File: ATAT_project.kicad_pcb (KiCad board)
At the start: 2 copper layers, 26 parts, among them SW1 SW_Push, SW2 SW_Push, U1 STM32F446RETx, U2 SPBTLE-RF

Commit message: scuffed but done
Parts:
- removed TP2: Test_VDDA, TestPoint:TestPoint_Keystone_5010-5014_Multipurpose
- added C12: 100p, Capacitor_SMD:C_0805_2012Metric_Pad1.18x1.45mm_HandSolder, F.Cu at (135.3, 50.7)
- added C13: 1u, Capacitor_SMD:C_0805_2012Metric_Pad1.18x1.45mm_HandSolder, F.Cu at (140.6, 50.7)
- added G***: LOGO, test:test5, F.Cu at (98.0, 57.7)
- C8: moved to F.Cu
- moved UART1 52.9 mm to (99.0, 83.4), turned to 90 degrees
- moved PWM_Channels1 50.4 mm to (89.9, 76.4), turned to 180 degrees
- moved U2 46.8 mm to (135.4, 56.0), turned to 180 degrees
- moved TP1 37.2 mm to (125.5, 70.0)
- moved TP5 30.9 mm to (114.3, 75.2)
- moved TP7 26.4 mm to (121.4, 74.3)
- moved TP3 26.1 mm to (95.0, 83.4)
- moved SW2 25.1 mm to (131.9, 83.7)
- moved TP6 23.8 mm to (107.1, 75.4)
- moved TP4 21.7 mm to (90.5, 83.4)
- moved SW1 16.9 mm to (142.3, 83.6)
- moved 2x5_stlinkv2 15.0 mm to (110.3, 83.3)
- moved C3 5.79 mm to (112.0, 59.5)
- moved C11 3.41 mm to (107.6, 56.1)
- moved C9 2.91 mm to (121.9, 60.9), turned to -90 degrees
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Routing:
- net +3V3: track 0.00 -> 142.0 mm, vias 0 -> 11
- net Net-(PWM_Channels1-Pin_10): track 0.00 -> 58.6 mm, vias 0 -> 3
- net Net-(PWM_Channels1-Pin_1): track 0.00 -> 43.3 mm, vias 0 -> 1
- net Net-(U1-PC2): track 0.00 -> 36.9 mm, vias 0 -> 1
- net Net-(PWM_Channels1-Pin_4): track 0.00 -> 36.8 mm, vias 0 -> 1
- net Net-(U1-PB10): track 0.00 -> 36.6 mm, vias 0 -> 2
- net Net-(PWM_Channels1-Pin_9): track 0.00 -> 36.3 mm, vias 0 -> 3
- net Net-(PWM_Channels1-Pin_2): track 0.00 -> 35.3 mm
- net Net-(PWM_Channels1-Pin_3): track 0.00 -> 34.4 mm, vias 0 -> 1
- net Net-(PWM_Channels1-Pin_5): track 0.00 -> 31.6 mm, vias 0 -> 1
- net Net-(U1-NRST): track 0.00 -> 31.4 mm
- net Net-(PWM_Channels1-Pin_6): track 0.00 -> 27.5 mm, vias 0 -> 1
- net Net-(U1-PA7): track 0.00 -> 24.6 mm, vias 0 -> 2
- net /swdio: track 0.00 -> 23.8 mm, vias 0 -> 2
- net Net-(U1-PB12): track 0.00 -> 23.6 mm, vias 0 -> 2
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- added copper zone on B.Cu, net GND
- added copper zone on F.Cu, net GND
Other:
- board outline added: 56.2 x 37.9 mm

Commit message: Fixed all DRC, started Casey's feedback
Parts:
- removed TP5: Test_swdio, TestPoint:TestPoint_Keystone_5010-5014_Multipurpose
- removed TP6: Test_swclk, TestPoint:TestPoint_Keystone_5010-5014_Multipurpose
- added GND1: Test_GND, TestPoint:TestPoint_Keystone_5010-5014_Multipurpose, F.Cu at (112.8, 74.6)
- added R1: 10k, Resistor_SMD:R_0805_2012Metric_Pad1.20x1.40mm_HandSolder, F.Cu at (138.0, 86.0)
- added R2: 10k, Resistor_SMD:R_0805_2012Metric_Pad1.20x1.40mm_HandSolder, F.Cu at (133.5, 86.0)
- PWM_Channels1: footprint Connector_PinHeader_2.54mm:PinHeader_1x11_P2.54mm_Vertical -> Connector_PinSocket_2.54mm:PinSocket_1x11_P2.54mm_Vertical
- UART1: value Conn_01x03_Female -> Conn_01x06_Socket; footprint Connector_PinHeader_2.54mm:PinHeader_1x03_P2.54mm_Vertical -> Connector_PinSocket_2.54mm:PinSocket_1x06_P2.54mm_Vertical
- moved RX1 16.3 mm to (105.3, 76.6)
- moved TX1 7.82 mm to (101.8, 79.6)
- moved UART1 2.91 mm to (101.8, 84.1), turned to -90 degrees
- moved C8 2.31 mm to (119.3, 57.6)
- moved FB1 2.06 mm to (122.8, 58.6)
- moved C6 2.05 mm to (116.8, 69.8)
- moved U2 2.05 mm to (133.6, 57.1)
- moved C12 2.05 mm to (133.6, 51.8)
- moved C13 2.05 mm to (138.9, 51.8)
- moved C4 2.05 mm to (115.1, 57.7)
- moved VDD1 2.05 mm to (123.7, 71.1)
- moved Button1 2.05 mm to (119.7, 75.4)
- moved C1 2.05 mm to (119.9, 66.1)
- moved C2 2.05 mm to (116.3, 54.2)
- moved C3 2.05 mm to (110.3, 60.6)
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- renumbered TP7 to Button1, SW1 to RESET1, TP4 to RX1, SW2 to Start/Stop1, TP3 to TX1, TP1 to VDD1, 2x5_stlinkv2 to stlinkv2
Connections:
- C7 pad 1: +3V3 -> Net-(C7-Pad1)
- C8 pad 1: +3V3 -> Net-(C7-Pad1)
- C9 pad 1: Net-(C9-Pad1) -> Net-(C7-Pad1)
- FB1 pad 2: Net-(C9-Pad1) -> Net-(C7-Pad1)
- UART1 pad 1: /TX -> unconnected-(UART1-Pin_1-Pad1)
- UART1 pad 3: GND -> /TX
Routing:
- net GND: track 22.0 -> 127.0 mm, vias 7 -> 13
- net /RX: track 0.00 -> 38.2 mm, vias 0 -> 2
- net /TX: track 0.00 -> 34.0 mm, vias 0 -> 2
- net Net-(C7-Pad1): track 0.00 -> 16.2 mm, vias 0 -> 3
- net Net-(PWM_Channels1-Pin_9): track 36.3 -> 46.2 mm
- net Net-(PWM_Channels1-Pin_10): track 58.6 -> 49.3 mm, vias 3 -> 1
- net Net-(U1-NRST): track 31.4 -> 39.3 mm
- net Net-(C9-Pad1): track 3.60 -> 0.00 mm
- net Net-(U1-PB12): track 23.6 -> 26.5 mm
- net +3V3: track 142.0 -> 139.4 mm, vias 11 -> 9
- net +3.3V: track 0.00 -> 2.50 mm
- net Net-(U1-PA5): track 23.6 -> 22.0 mm
- net /swclk: track 14.7 -> 16.0 mm
- net Net-(PWM_Channels1-Pin_1): track 43.3 -> 42.0 mm
- net Net-(U1-PC2): track 36.9 -> 37.9 mm
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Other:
- board text added: "ATAT Walker PCB ECE395 Fall 2024 Joseph C, Eddie D, Frank F"

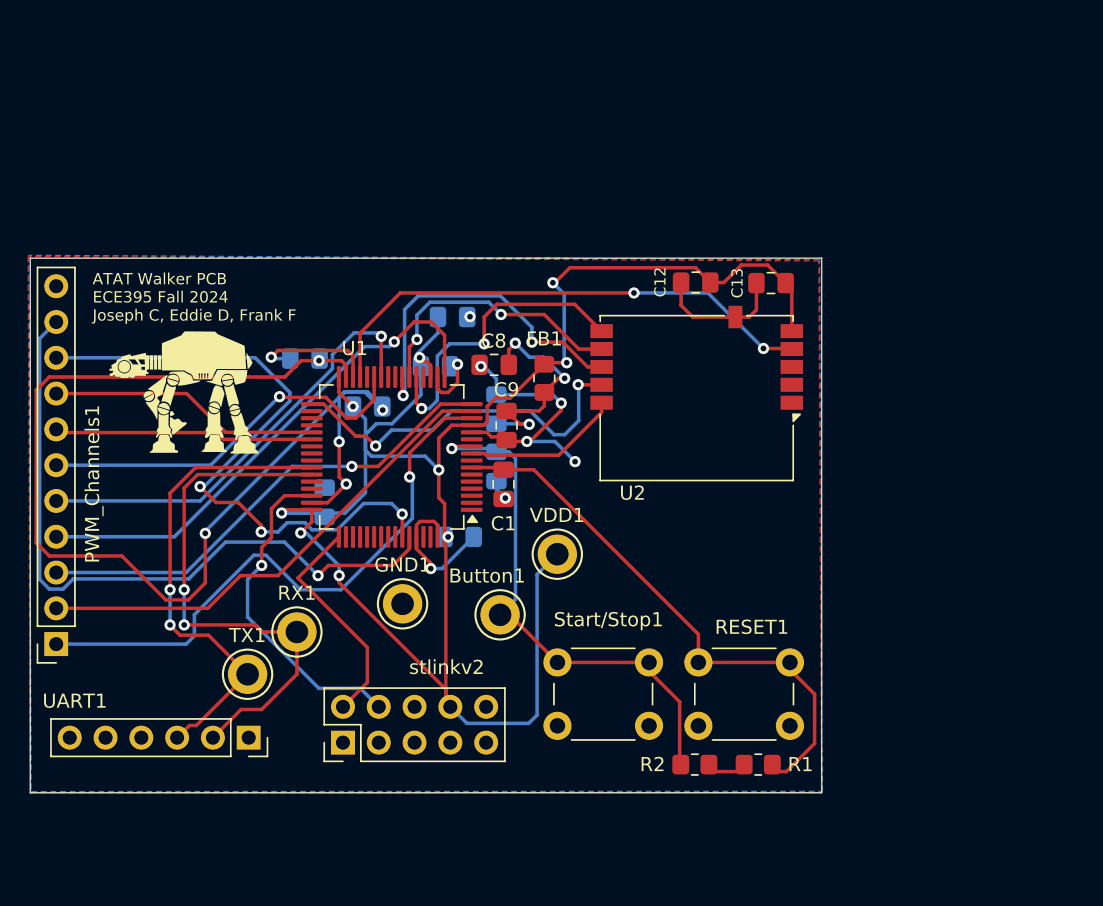
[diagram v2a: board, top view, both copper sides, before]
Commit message: NEW SCHEMATIC! (Needs PCB Design)
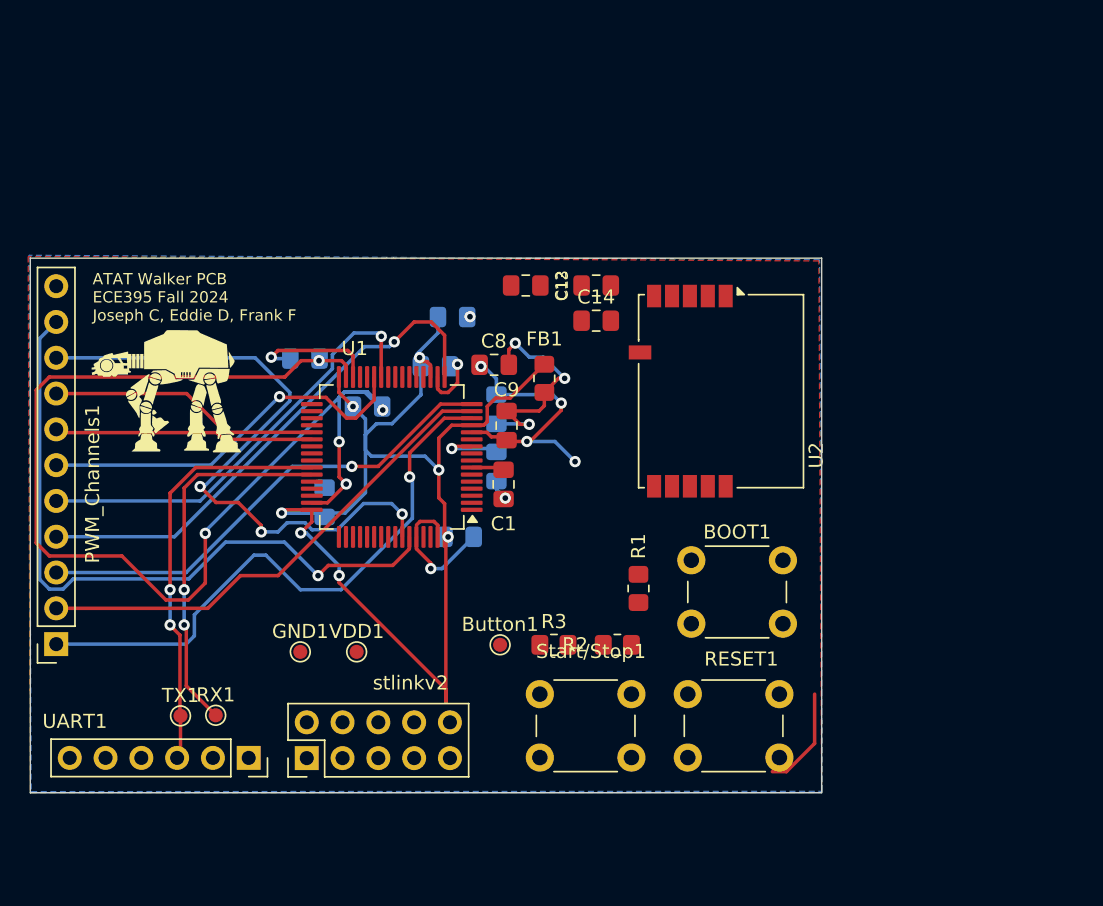
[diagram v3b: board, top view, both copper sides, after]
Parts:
- added BOOT1: SW_Push, Button_Switch_THT:SW_PUSH_6mm_H4.3mm, F.Cu at (133.2, 71.5)
- added C14: 0.1u, Capacitor_SMD:C_0805_2012Metric_Pad1.18x1.45mm_HandSolder, F.Cu at (126.5, 54.5)
- added R3: 10k, Resistor_SMD:R_0805_2012Metric_Pad1.20x1.40mm_HandSolder, F.Cu at (123.5, 77.5)
- Button1, GND1, RX1, TX1, VDD1: footprint TestPoint:TestPoint_Keystone_5010-5014_Multipurpose -> TestPoint:TestPoint_Pad_D1.0mm
- moved VDD1 15.8 mm to (109.5, 78.0)
- moved R1 15.1 mm to (129.5, 73.5), turned to 90 degrees
- moved C13 12.4 mm to (126.5, 52.0)
- moved C12 12.1 mm to (121.5, 52.0), turned to 180 degrees
- moved R2 10.1 mm to (128.0, 77.5)
- moved RX1 8.25 mm to (99.5, 82.5)
- moved GND1 8.02 mm to (105.5, 78.0)
- moved TX1 5.60 mm to (97.0, 82.5)
- moved stlinkv2 2.80 mm to (106.0, 85.5)
- moved U2 2.63 mm to (132.5, 59.5), turned to -90 degrees
- moved Start/Stop1 2.57 mm to (129.0, 85.5)
- moved RESET1 2.37 mm to (139.5, 85.5)
- moved Button1 2.13 mm to (119.7, 77.5)
- moved UART1 1.44 mm to (101.8, 85.5)
- moved G*** 1.26 mm to (96.0, 59.5)
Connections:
- C7 pad 1: Net-(C7-Pad1) -> +3V3
- C8 pad 1: Net-(C7-Pad1) -> +3V3
- C9 pad 1: Net-(C7-Pad1) -> +3V3
- FB1 pad 2: Net-(C7-Pad1) -> +3V3
- U1 pad 1: unconnected-(U1-VBAT-Pad1) -> +3V3
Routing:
- net Net-(U1-NRST): track 39.3 -> 2.32 mm
- net Net-(U1-PB10): track 36.6 -> 0.00 mm, vias 2 -> 0
- net Net-(U1-PC2): track 37.9 -> 4.75 mm
- net +3V3: track 139.4 -> 106.3 mm, vias 9 -> 10
- net Net-(U1-PB12): track 26.5 -> 0.00 mm, vias 2 -> 0
- net Net-(U1-PA7): track 24.6 -> 0.00 mm, vias 2 -> 0
- net /swdio: track 23.6 -> 0.00 mm, vias 1 -> 0
- net Net-(U1-PA5): track 22.0 -> 0.00 mm, vias 2 -> 0
- net Net-(U1-PA6): track 19.5 -> 0.00 mm, vias 2 -> 0
- net Net-(C7-Pad1): track 16.2 -> 0.00 mm, vias 3 -> 0
- net /swclk: track 16.0 -> 0.00 mm
- net /RX: track 38.2 -> 26.2 mm
- net Net-(U1-PC1): track 11.2 -> 0.00 mm
- net /TX: track 34.0 -> 29.9 mm
- net +3.3V: track 2.50 -> 0.00 mm
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
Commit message: NEW PCB!!!
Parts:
- removed PWM_Channels1: Conn_01x11_Female, Connector_PinSocket_2.54mm:PinSocket_1x11_P2.54mm_Vertical
- added 5V1: Test_5V, TestPoint:TestPoint_Pad_D1.0mm, F.Cu at (151.5, 54.5)
- added C15: 100n, Capacitor_SMD:C_0805_2012Metric_Pad1.18x1.45mm_HandSolder, F.Cu at (109.0, 65.5)
- added J1: Conn_01x03_Socket, Connector_PinSocket_2.54mm:PinSocket_1x03_P2.54mm_Vertical, F.Cu at (155.5, 49.0)
- added PWM1: Conn_01x03_Pin, Connector_PinHeader_2.54mm:PinHeader_1x03_P2.54mm_Vertical, F.Cu at (142.0, 54.0)
- added PWM10: Conn_01x03_Pin, Connector_PinHeader_2.54mm:PinHeader_1x03_P2.54mm_Vertical, F.Cu at (100.2, 54.0)
- added PWM2: Conn_01x03_Pin, Connector_PinHeader_2.54mm:PinHeader_1x03_P2.54mm_Vertical, F.Cu at (137.3, 54.0)
- added PWM3: Conn_01x03_Pin, Connector_PinHeader_2.54mm:PinHeader_1x03_P2.54mm_Vertical, F.Cu at (132.7, 54.0)
- added PWM4: Conn_01x03_Pin, Connector_PinHeader_2.54mm:PinHeader_1x03_P2.54mm_Vertical, F.Cu at (128.1, 54.0)
- added PWM5: Conn_01x03_Pin, Connector_PinHeader_2.54mm:PinHeader_1x03_P2.54mm_Vertical, F.Cu at (123.4, 54.0)
- added PWM6: Conn_01x03_Pin, Connector_PinHeader_2.54mm:PinHeader_1x03_P2.54mm_Vertical, F.Cu at (118.8, 54.0)
- added PWM7: Conn_01x03_Pin, Connector_PinHeader_2.54mm:PinHeader_1x03_P2.54mm_Vertical, F.Cu at (114.1, 54.0)
- added PWM8: Conn_01x03_Pin, Connector_PinHeader_2.54mm:PinHeader_1x03_P2.54mm_Vertical, F.Cu at (109.5, 54.0)
- added PWM9: Conn_01x03_Pin, Connector_PinHeader_2.54mm:PinHeader_1x03_P2.54mm_Vertical, F.Cu at (104.8, 54.0)
- added TP1: Test_PWM, TestPoint:TestPoint_Pad_D1.0mm, F.Cu at (142.2, 58.5)
- added TP10: Test_PWM, TestPoint:TestPoint_Pad_D1.0mm, F.Cu at (100.2, 58.5)
- added TP2: Test_PWM, TestPoint:TestPoint_Pad_D1.0mm, F.Cu at (137.7, 58.5)
- added TP3: Test_PWM, TestPoint:TestPoint_Pad_D1.0mm, F.Cu at (133.2, 58.5)
- added TP4: Test_PWM, TestPoint:TestPoint_Pad_D1.0mm, F.Cu at (128.7, 58.5)
- added TP5: Test_PWM, TestPoint:TestPoint_Pad_D1.0mm, F.Cu at (123.7, 58.5)
- added TP6: Test_PWM, TestPoint:TestPoint_Pad_D1.0mm, F.Cu at (119.2, 58.5)
- added TP7: Test_PWM, TestPoint:TestPoint_Pad_D1.0mm, F.Cu at (114.7, 58.5)
- added TP8: Test_PWM, TestPoint:TestPoint_Pad_D1.0mm, F.Cu at (110.2, 58.5)
- added TP9: Test_PWM, TestPoint:TestPoint_Pad_D1.0mm, F.Cu at (105.2, 58.5)
- C10, C11, C2, C3, C4, C5, C6, C7: moved to F.Cu
- moved GND1 53.1 mm to (151.5, 51.5), turned to 180 degrees
- moved VDD1 51.3 mm to (151.5, 48.5), turned to 180 degrees
- moved stlinkv2 48.6 mm to (154.5, 87.5), turned to -90 degrees
- moved G*** 45.4 mm to (139.0, 74.0)
- moved C14 25.5 mm to (112.0, 75.5), turned to 90 degrees
- moved C12 24.8 mm to (143.5, 63.5), turned to -90 degrees
- moved C11 23.6 mm to (116.0, 78.5)
- moved C13 20.8 mm to (145.5, 60.5)
- moved Button1 20.0 mm to (103.0, 88.5), turned to 90 degrees
- moved UART1 19.7 mm to (100.0, 65.9), turned to 0 degrees
- moved U2 19.3 mm to (148.8, 69.8)
- moved C8 19.2 mm to (136.0, 67.0), turned to -90 degrees
- moved R2 18.8 mm to (110.0, 83.0), turned to 0 degrees
- moved Start/Stop1 17.1 mm to (112.8, 90.8)
- moved RESET1 15.2 mm to (125.2, 90.8)
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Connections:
- net Net-(U1-PA5) renamed SPI_CLK
- net Net-(U1-PA6) renamed SPI_MISO
- net Net-(U1-PA7) renamed SPI_MOSI
- net Net-(U1-PB10) renamed SPI_IRQ
- net Net-(U1-PB12) renamed SPI_CS
- net Net-(U1-PC1) renamed BT_RESET
- C12 pad 2: +3V3 -> +3.3V
- C13 pad 2: +3V3 -> +3.3V
- C2 pad 1: +3V3 -> +3.3V
- C3 pad 1: +3V3 -> +3.3V
- C4 pad 1: +3V3 -> +3.3V
- C5 pad 1: +3V3 -> +3.3V
- C6 pad 1: +3V3 -> +3.3V
- C7 pad 1: +3V3 -> +3.3V
- C8 pad 1: +3V3 -> +3.3V
- C9 pad 1: +3V3 -> +3.3V
- FB1 pad 1: +3V3 -> +3.3V
- FB1 pad 2: +3V3 -> +3.3V
- RX1 pad 1: /RX -> /MCU_RX
- TX1 pad 1: /TX -> /MCU_TX
- U1 pad 1: +3V3 -> +3.3V
- U1 pad 13: +3V3 -> +3.3V
- U1 pad 14: Net-(PWM_Channels1-Pin_1) -> PWM1
- U1 pad 15: Net-(PWM_Channels1-Pin_2) -> PWM2
- U1 pad 16: Net-(PWM_Channels1-Pin_3) -> PWM3
- U1 pad 17: Net-(PWM_Channels1-Pin_4) -> PWM4
- U1 pad 19: +3V3 -> +3.3V
- U1 pad 26: Net-(PWM_Channels1-Pin_5) -> PWM5
- U1 pad 27: Net-(PWM_Channels1-Pin_6) -> PWM6
- U1 pad 32: +3V3 -> +3.3V
- U1 pad 37: Net-(PWM_Channels1-Pin_8) -> PWM8
- U1 pad 38: Net-(PWM_Channels1-Pin_7) -> PWM7
- U1 pad 42: /TX -> /MCU_TX
- U1 pad 43: /RX -> /MCU_RX
- U1 pad 48: +3V3 -> +3.3V
- U1 pad 58: Net-(PWM_Channels1-Pin_9) -> PWM9
- U1 pad 59: Net-(PWM_Channels1-Pin_10) -> PWM10
- U1 pad 64: +3V3 -> +3.3V
- U2 pad 5: +3V3 -> +3.3V
- UART1 pad 1: unconnected-(UART1-Pin_1-Pad1) -> GND
- UART1 pad 2: /RX -> unconnected-(UART1-Pin_2-Pad2)
- UART1 pad 3: /TX -> unconnected-(UART1-Pin_3-Pad3)
- UART1 pad 4: unconnected-(UART1-Pin_4-Pad4) -> /MCU_RX
- UART1 pad 5: unconnected-(UART1-Pin_5-Pad5) -> /MCU_TX
- UART1 pad 6: GND -> unconnected-(UART1-Pin_6-Pad6)
- VDD1 pad 1: +3V3 -> +3.3V
- stlinkv2 pad 8: +3V3 -> +3.3V
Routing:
- net GND: track 124.9 -> 360.3 mm, vias 13 -> 2
- net +3.3V: track 0.00 -> 178.8 mm, vias 0 -> 2
- net +3V3: track 106.3 -> 0.00 mm, vias 10 -> 0
- net /swdio: track 0.00 -> 90.8 mm, vias 0 -> 2
- net Net-(U1-PC2): track 4.75 -> 91.2 mm, vias 1 -> 2
- net SPI_IRQ: track 0.00 -> 67.8 mm, vias 0 -> 2
- net Net-(BOOT1-Pad1): track 0.00 -> 60.6 mm
- net SPI_CS: track 0.00 -> 57.9 mm, vias 0 -> 2
- net PWM9: track 0.00 -> 57.0 mm, vias 0 -> 2
- net +5V: track 0.00 -> 56.8 mm
- net Net-(PWM_Channels1-Pin_10): track 49.3 -> 0.00 mm, vias 1 -> 0
- net Net-(U1-NRST): track 2.32 -> 48.5 mm, vias 0 -> 4
- net Net-(PWM_Channels1-Pin_9): track 46.2 -> 0.00 mm, vias 3 -> 0
- net Net-(U1-VCAP_1): track 9.06 -> 53.0 mm, vias 1 -> 2
- net /swclk: track 0.00 -> 43.4 mm, vias 0 -> 2
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- added copper zone on F.Cu, net (none)
- added copper zone on B.Cu, net +3.3V
- removed copper zone on B.Cu, net GND
- removed copper zone on F.Cu, net GND
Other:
- board size 56.2 x 37.9 mm -> 61.5 x 47.5 mm
